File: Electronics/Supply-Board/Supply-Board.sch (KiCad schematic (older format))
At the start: 90 parts, among them J1 DB25_Female_MountingHoles, J2 PE, J3 L, J4 N, T1 VC 5,0/2/15, T2 VC 5,0/2/18, U1 LM317, U2 LM337, U3 240R, U4 LM337, U5 traco_TSR_0.5-2433, U6 LM75C

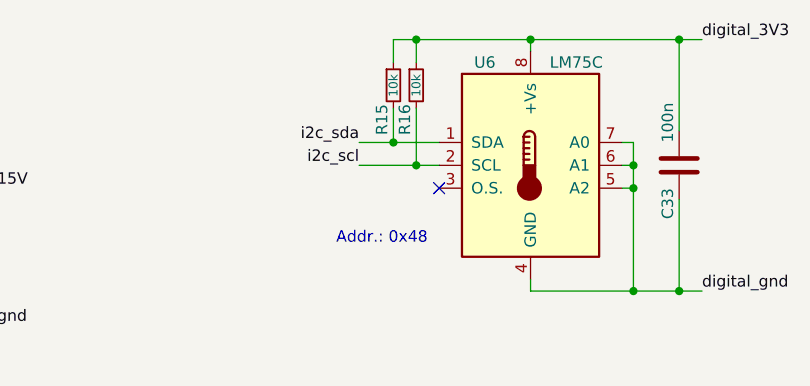
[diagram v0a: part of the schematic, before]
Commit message: Added images
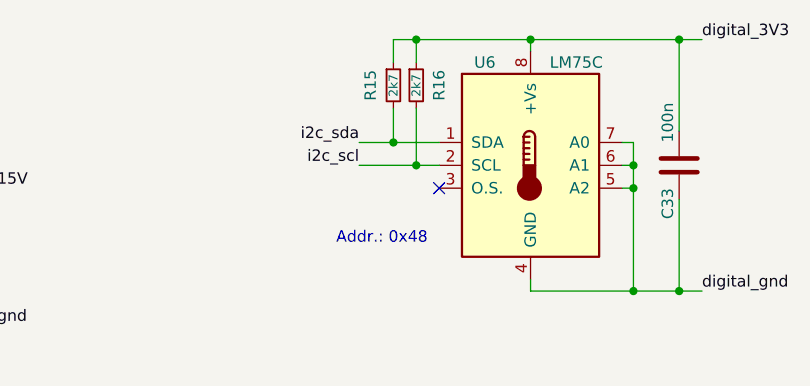
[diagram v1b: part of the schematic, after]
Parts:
- R15, R16: value 10k -> 2k7
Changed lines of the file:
@@
 U 1 1 5E6AC065
 P 8650 1100
-F 0 "R16" V 8600 950 50  0000 C CNN
-F 1 "10k" V 8650 1050 39  0000 L CNN
+F 0 "R16" V 8750 1100 50  0000 C CNN
+F 1 "2k7" V 8650 1050 39  0000 L CNN
 F 2 "Resistor_SMD:R_0805_2012Metric_Pad1.15x1.40mm_HandSolder" H 8650 1100 50  0001 C CNN
 F 3 "~" H 8650 1100 50  0001 C CNN
 	1    8650 1100
-	1    0    0    -1
-$EndComp
-$Comp
-L Device:R_Small R15
-U 1 1 5E6AB696
-P 8550 1100
-F 0 "R15" V 8500 950 50  0000 C CNN
-F 1 "10k" V 8550 1050 39  0000 L CNN
-F 2 "Resistor_SMD:R_0805_2012Metric_Pad1.15x1.40mm_HandSolder" H 8550 1100 50  0001 C CNN
-F 3 "~" H 8550 1100 50  0001 C CNN
-	1    8550 1100
 	1    0    0    -1
 $EndComp
@@
 Text Notes 2900 5250 0    50   ~ 0
 max. 2 A
+$Comp
+L Device:R_Small R15
+U 1 1 5E6AB696
+P 8550 1100
+F 0 "R15" V 8450 1100 50  0000 C CNN
+F 1 "2k7" V 8550 1050 39  0000 L CNN
+F 2 "Resistor_SMD:R_0805_2012Metric_Pad1.15x1.40mm_HandSolder" H 8550 1100 50  0001 C CNN
+F 3 "~" H 8550 1100 50  0001 C CNN
+	1    8550 1100
+	1    0    0    -1
+$EndComp
 $EndSCHEMATC

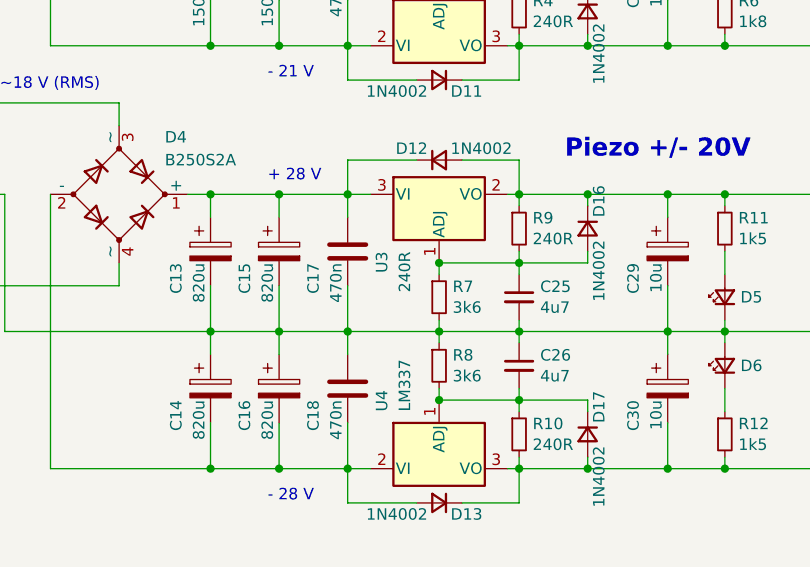
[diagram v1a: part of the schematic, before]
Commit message: Fixed values in schematic
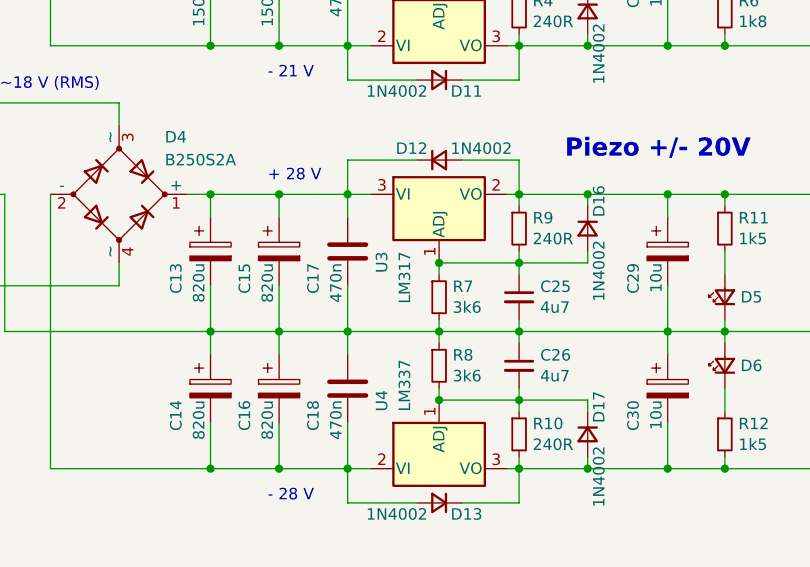
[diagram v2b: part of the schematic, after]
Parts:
- L1: Reichelt (none) -> L-PISM 3,3µ
- U3: value 240R -> LM317
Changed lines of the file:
@@
 P 4900 3400
 F 0 "U3" V 4650 3150 50  0000 R CNN
-F 1 "240R" V 4750 3150 50  0000 R CNN
+F 1 "LM317" V 4750 3150 50  0000 R CNN
 F 2 "Package_TO_SOT_SMD:TO-252-2" H 4900 3650 50  0001 C CIN
 F 3 "http://www.ti.com/lit/ds/symlink/lm317.pdf" H 4900 3400 50  0001 C CNN
@@
 F 1 "3u3" V 4844 5300 50  0000 C CNN
 F 2 "Inductor_SMD:L_Fastron_PISN_Handsoldering" H 4750 5300 50  0001 C CNN
-F 3 "~" H 4750 5300 50  0001 C CNN
+F 3 "https://cdn-reichelt.de/documents/datenblatt/B400/PISM.pdf" H 4750 5300 50  0001 C CNN
+F 4 "L-PISM 3,3µ" V 4750 5300 50  0001 C CNN "Reichelt"
 	1    4750 5300
 	0    -1   -1   0
